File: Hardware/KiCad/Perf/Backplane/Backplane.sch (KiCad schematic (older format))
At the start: 10 parts, among them P1 CONN_02X20, P2 CONN_02X20, P3 CONN_02X16, P4 CONN_02X16, P5 CONN_02X16, P6 CONN_02X16, P7 CONN_02X16, P8 CONN_02X16, P9 CONN_02X16

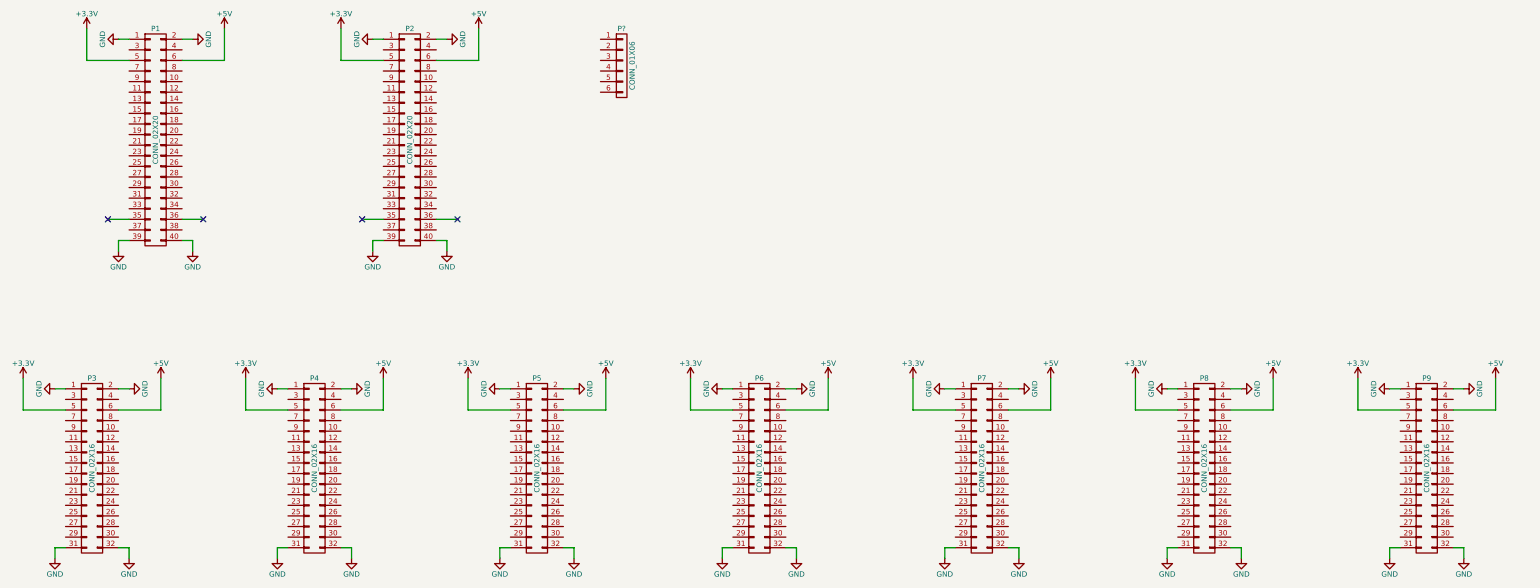
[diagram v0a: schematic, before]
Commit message: laying out motherboard and backplane
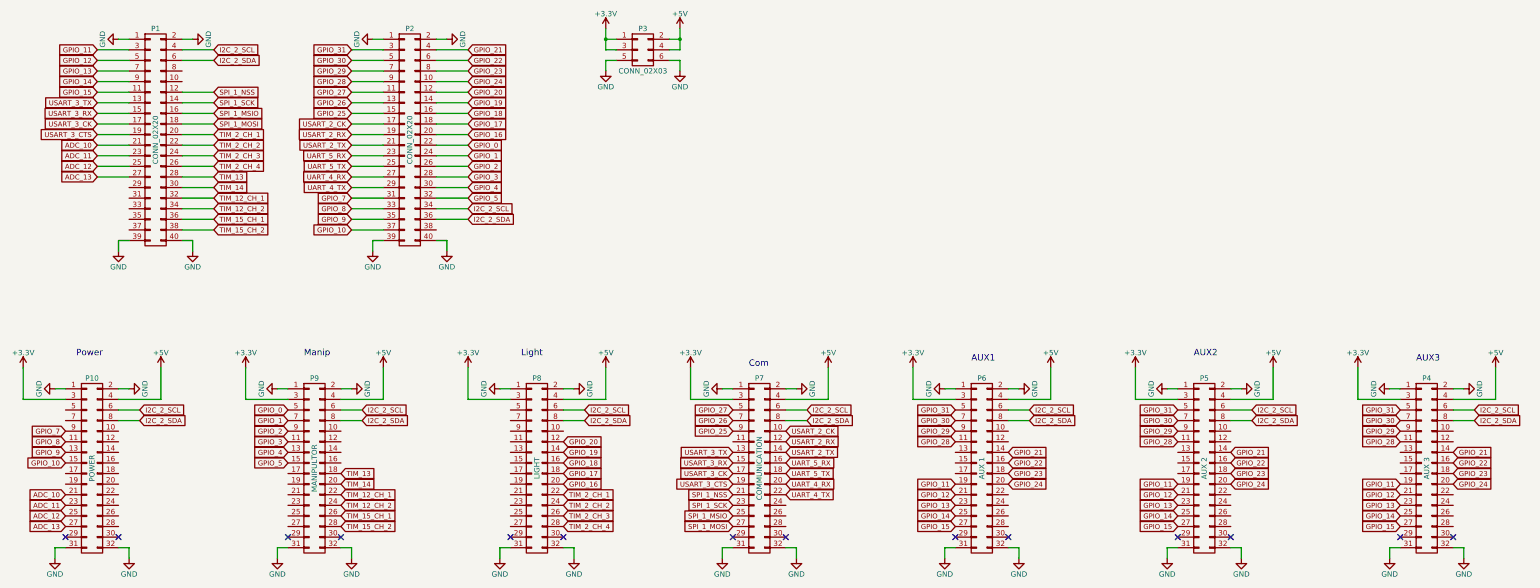
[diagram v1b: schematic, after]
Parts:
- removed P?: CONN_01X06, symbol CONN_01X06
- added P3: CONN_02X03, symbol CONN_02X03
- P10: renamed from P4; value CONN_02X16 -> POWER
- P4: renamed from P3; value CONN_02X16 -> AUX 3
- P5: renamed from P9; value CONN_02X16 -> AUX 2
- P6: renamed from P8; value CONN_02X16 -> AUX 1
- P7: value CONN_02X16 -> COMMUNICATION
- P8: renamed from P6; value CONN_02X16 -> LIGHT
- P9: renamed from P5; value CONN_02X16 -> MANIPULTOR
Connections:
- net +3V3: now also P10.3 (P3), P4.3 (P3), P5.3 (P3), P6.3 (P3), P7.3 (P3), P8.3 (P3), P9.3 (P3), P3.1 (P1), P3.3 (P3); no longer P1.5 (P5), P10.5 (P5), P2.5 (P5), P4.5 (P5), P5.5 (P5), P6.5 (P5), P7.5 (P5), P8.5 (P5), P9.5 (P5)
- net +5V: now also P10.4 (P4), P4.4 (P4), P5.4 (P4), P6.4 (P4), P7.4 (P4), P8.4 (P4), P9.4 (P4), P3.2 (P2), P3.4 (P4); no longer P1.6 (P6), P10.6 (P6), P2.6 (P6), P4.6 (P6), P5.6 (P6), P6.6 (P6), P7.6 (P6), P8.6 (P6), P9.6 (P6)
- net GND: now also P3.5 (P5), P3.6 (P6)
- net GPIO_28: now reaches P4.11 (P11)
- net GPIO_28: now also P2.9 (P9), P5.11 (P11), P6.11 (P11)
- net GPIO_21: now reaches P4.14 (P14)
- net GPIO_21: now also P2.4 (P4), P5.14 (P14), P6.14 (P14)
- net GPIO_22: now reaches P4.16 (P16)
- net GPIO_22: now also P2.6 (P6), P5.16 (P16), P6.16 (P16)
- net GPIO_23: now reaches P4.18 (P18)
- net GPIO_23: now also P2.8 (P8), P5.18 (P18), P6.18 (P18)
- net GPIO_11: now reaches P4.19 (P19)
- net GPIO_11: now also P1.3 (P3), P5.19 (P19), P6.19 (P19)
- net GPIO_24: now reaches P4.20 (P20)
- net GPIO_24: now also P2.10 (P10), P5.20 (P20), P6.20 (P20)
- net GPIO_12: now reaches P4.21 (P21)
- net GPIO_12: now also P1.5 (P5), P5.21 (P21), P6.21 (P21)
- net GPIO_13: now reaches P4.23 (P23)
- net GPIO_13: now also P1.7 (P7), P5.23 (P23), P6.23 (P23)
- net GPIO_14: now reaches P4.25 (P25)
- net GPIO_14: now also P1.9 (P9), P5.25 (P25), P6.25 (P25)
- net GPIO_15: now reaches P4.27 (P27)
- net GPIO_15: now also P1.11 (P11), P5.27 (P27), P6.27 (P27)
- net GPIO_30: now reaches P4.7 (P7)
- net GPIO_30: now also P2.5 (P5), P5.7 (P7), P6.7 (P7)
- net I2C_2_SDA: now reaches P4.8 (P8)
- net I2C_2_SDA: now also P1.6 (P6), P10.8 (P8), P2.36 (P36), P5.8 (P8), P6.8 (P8), P7.8 (P8), P8.8 (P8), P9.8 (P8)
- net GPIO_29: now reaches P4.9 (P9)
- net GPIO_29: now also P2.7 (P7), P5.9 (P9), P6.9 (P9)
- net GPIO_8: now reaches P10.11 (P11)
- net GPIO_8: now also P2.33 (P33)
- net GPIO_9: now reaches P10.13 (P13)
- net GPIO_9: now also P2.35 (P35)
- net GPIO_10: now reaches P10.15 (P15)
- net GPIO_10: now also P2.37 (P37)
- net ADC_10: now reaches P10.21 (P21)
- net ADC_10: now also P1.21 (P21)
- net ADC_11: now reaches P10.23 (P23)
- net ADC_11: now also P1.23 (P23)
- net ADC_12: now reaches P10.25 (P25)
- net ADC_12: now also P1.25 (P25)
- net ADC_13: now reaches P10.27 (P27)
- net ADC_13: now also P1.27 (P27)
- net GPIO_7: now reaches P10.9 (P9)
- net GPIO_7: now also P2.31 (P31)
- net GPIO_3: now reaches P9.11 (P11)
- net GPIO_3: now also P2.28 (P28)
- net GPIO_4: now reaches P9.13 (P13)
- net GPIO_4: now also P2.30 (P30)
- net GPIO_5: now reaches P9.15 (P15)
- net GPIO_5: now also P2.32 (P32)
- net TIM_13: now reaches P9.18 (P18)
- net TIM_13: now also P1.28 (P28)
- net TIM_14: now reaches P9.20 (P20)
- net TIM_14: now also P1.30 (P30)
- net TIM_12_CH_1: now reaches P9.22 (P22)
- net TIM_12_CH_1: now also P1.32 (P32)
- net TIM_12_CH_2: now reaches P9.24 (P24)
- net TIM_12_CH_2: now also P1.34 (P34)
- net TIM_15_CH_1: now reaches P9.26 (P26)
- net TIM_15_CH_1: now also P1.36 (P36)
- net TIM_15_CH_2: now reaches P9.28 (P28)
- net TIM_15_CH_2: now also P1.38 (P38)
- net GPIO_1: now reaches P9.7 (P7)
- net GPIO_1: now also P2.24 (P24)
- net GPIO_2: now reaches P9.9 (P9)
- net GPIO_2: now also P2.26 (P26)
- net GPIO_20: now reaches P8.12 (P12)
- net GPIO_20: now also P2.12 (P12)
- net GPIO_19: now reaches P8.14 (P14)
- net GPIO_19: now also P2.14 (P14)
- net GPIO_18: now reaches P8.16 (P16)
- net GPIO_18: now also P2.16 (P16)
- net GPIO_17: now reaches P8.18 (P18)
- net GPIO_17: now also P2.18 (P18)
- net GPIO_16: now reaches P8.20 (P20)
- net GPIO_16: now also P2.20 (P20)
- net TIM_2_CH_1: now reaches P8.22 (P22)
- net TIM_2_CH_1: now also P1.20 (P20)
- net TIM_2_CH_2: now reaches P8.24 (P24)
- net TIM_2_CH_2: now also P1.22 (P22)
- net TIM_2_CH_3: now reaches P8.26 (P26)
- net TIM_2_CH_3: now also P1.24 (P24)
- net TIM_2_CH_4: now reaches P8.28 (P28)
- net TIM_2_CH_4: now also P1.26 (P26)
- net USART_2_CK: now reaches P7.10 (P10)
- net USART_2_CK: now also P2.17 (P17)
- net USART_2_RX: now reaches P7.12 (P12)
- net USART_2_RX: now also P2.19 (P19)
- net USART_3_TX: now reaches P7.13 (P13)
- net USART_3_TX: now also P1.13 (P13)
- net USART_2_TX: now reaches P7.14 (P14)
- net USART_2_TX: now also P2.21 (P21)
- net USART_3_RX: now reaches P7.15 (P15)
- net USART_3_RX: now also P1.15 (P15)
- net UART_5_RX: now reaches P7.16 (P16)
- net UART_5_RX: now also P2.23 (P23)
- net USART_3_CK: now reaches P7.17 (P17)
- net USART_3_CK: now also P1.17 (P17)
- net UART_5_TX: now reaches P7.18 (P18)
- net UART_5_TX: now also P2.25 (P25)
- net USART_3_CTS: now reaches P7.19 (P19)
- net USART_3_CTS: now also P1.19 (P19)
- net UART_4_RX: now reaches P7.20 (P20)
- net UART_4_RX: now also P2.27 (P27)
- net SPI_1_NSS: now reaches P7.21 (P21)
- net SPI_1_NSS: now also P1.12 (P12)
- net UART_4_TX: now reaches P7.22 (P22)
- net UART_4_TX: now also P2.29 (P29)
- net SPI_1_SCK: now reaches P7.23 (P23)
- net SPI_1_SCK: now also P1.14 (P14)
- net SPI_1_MSIO: now reaches P7.25 (P25)
- net SPI_1_MSIO: now also P1.16 (P16)
- net SPI_1_MOSI: now reaches P7.27 (P27)
- net SPI_1_MOSI: now also P1.18 (P18)
- net GPIO_26: now reaches P7.7 (P7)
- net GPIO_26: now also P2.13 (P13)
- net GPIO_25: now reaches P7.9 (P9)
- net GPIO_25: now also P2.15 (P15)
- net I2C_2_SCL: now reaches P1.4 (P4)
- net I2C_2_SCL: now also P10.6 (P6), P2.34 (P34), P4.6 (P6), P5.6 (P6), P6.6 (P6), P7.6 (P6), P8.6 (P6), P9.6 (P6)
- net GPIO_27: now reaches P2.11 (P11)
- net GPIO_27: now also P7.5 (P5)
- net GPIO_0: now reaches P2.22 (P22)
- net GPIO_0: now also P9.5 (P5)
- net GPIO_31: now reaches P2.3 (P3)
- net GPIO_31: now also P4.5 (P5), P5.5 (P5), P6.5 (P5)
- no-connect marks 4 -> 14
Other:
- note added: "AUX1"
- note added: "AUX2"
- note added: "AUX3"
- note added: "Com"
- note added: "Light"
- note added: "Manip"
- note added: "Power"
- moved on the sheet: P10, P4, P5, P6, P7, P8, P9

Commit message: Small change to USART 2 pin layout from MB to Backplane
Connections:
- net GPIO_25: now also P2.11 (P11); no longer P2.15 (P15)
- net GPIO_26: now also P2.9 (P9); no longer P2.13 (P13)
- net GPIO_27: now also P2.7 (P7); no longer P2.11 (P11)
- net GPIO_28: now also P2.5 (P5); no longer P2.9 (P9)
- net GPIO_29: now also P2.3 (P3); no longer P2.7 (P7)
- net I2C_2_SCL: now also P1.8 (P8); no longer P1.4 (P4)
- net I2C_2_SDA: now also P1.10 (P10); no longer P1.6 (P6)
- net UART_4_RX: now also P7.24 (P24); no longer P7.20 (P20)
- net UART_4_TX: now also P7.26 (P26); no longer P7.22 (P22)
- net UART_5_RX: now also P7.20 (P20); no longer P7.16 (P16)
- net UART_5_TX: now also P7.22 (P22); no longer P7.18 (P18)
- net USART_2_CK: now also P2.13 (P13); no longer P2.17 (P17)
- net USART_2_RX: now also P2.15 (P15); no longer P2.19 (P19)
- net USART_2_TX: now also P2.17 (P17); no longer P2.21 (P21)
- removed net GPIO_30: P2.5 (P5), P4.7 (P7), P5.7 (P7), P6.7 (P7)
- removed net GPIO_31: P2.3 (P3), P4.5 (P5), P5.5 (P5), P6.5 (P5)
- new net USART_2_CTS: P2.21 (P21), P7.18 (P18)
- new net USART_2_RTS: P2.19 (P19), P7.16 (P16)
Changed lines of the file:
@@
 NoConn ~ 14500 6900
 NoConn ~ 15000 6900
-Text GLabel 3300 2300 2    47   Input ~ 0
-I2C_2_SCL
-Text GLabel 3300 2400 2    47   Input ~ 0
+Text GLabel 3300 2500 2    47   Input ~ 0
+I2C_2_SCL
+Text GLabel 3300 2600 2    47   Input ~ 0
 I2C_2_SDA
 Text GLabel 5700 3800 2    47   Input ~ 0
@@
 	15200 5800 15000 5800
 Wire Wire Line
-	3000 2300 3300 2300
-Wire Wire Line
-	3300 2400 3000 2400
+	3000 2500 3300 2500
+Wire Wire Line
+	3300 2600 3000 2600
 Wire Wire Line
 	5700 3800 5400 3800
@@
 Text GLabel 2200 3500 0    47   Input ~ 0
 ADC_13
+Text GLabel 4600 3200 0    47   Input ~ 0
+USART_2_CTS
+Text GLabel 4600 2900 0    47   Input ~ 0
+USART_2_RX
 Text GLabel 4600 3000 0    47   Input ~ 0
-USART_2_CK
-Text GLabel 4600 3100 0    47   Input ~ 0
-USART_2_RX
-Text GLabel 4600 3200 0    47   Input ~ 0
 USART_2_TX
 Text GLabel 4600 3300 0    47   Input ~ 0
@@
 GPIO_5
 Text GLabel 4600 2300 0    47   Input ~ 0
-GPIO_31
+GPIO_29
 Text GLabel 4600 2400 0    47   Input ~ 0
-GPIO_30
+GPIO_28
 Text GLabel 4600 2500 0    47   Input ~ 0
-GPIO_29
+GPIO_27
 Text GLabel 4600 2600 0    47   Input ~ 0
-GPIO_28
+GPIO_26
 Text GLabel 4600 2700 0    47   Input ~ 0
-GPIO_27
-Text GLabel 4600 2800 0    47   Input ~ 0
-GPIO_26
-Text GLabel 4600 2900 0    47   Input ~ 0
 GPIO_25
 Wire Wire Line
@@
 Text GLabel 12900 6400 2    47   Input ~ 0
 GPIO_24
-Text GLabel 12400 5700 0    47   Input ~ 0
-GPIO_31
-Text GLabel 12400 5800 0    47   Input ~ 0
-GPIO_30
 Text GLabel 12400 5900 0    47   Input ~ 0
 GPIO_29
@@
 Text GLabel 8700 6100 2    47   Input ~ 0
 USART_2_TX
-Text GLabel 8700 6200 2    47   Input ~ 0
+Text GLabel 8700 6400 2    47   Input ~ 0
 UART_5_RX
-Text GLabel 8700 6300 2    47   Input ~ 0
+Text GLabel 8700 6500 2    47   Input ~ 0
 UART_5_TX
-Text GLabel 8700 6400 2    47   Input ~ 0
+Text GLabel 8700 6600 2    47   Input ~ 0
 UART_4_RX
-Text GLabel 8700 6500 2    47   Input ~ 0
+Text GLabel 8700 6700 2    47   Input ~ 0
 UART_4_TX
 Text GLabel 10300 6400 0    47   Input ~ 0
@@
 Text GLabel 10300 6800 0    47   Input ~ 0
 GPIO_15
-Text GLabel 10300 5700 0    47   Input ~ 0
-GPIO_31
-Text GLabel 10300 5800 0    47   Input ~ 0
-GPIO_30
 Text GLabel 10300 5900 0    47   Input ~ 0
 GPIO_29
@@
 Text GLabel 14500 6800 0    47   Input ~ 0
 GPIO_15
-Text GLabel 14500 5700 0    47   Input ~ 0
-GPIO_31
-Text GLabel 14500 5800 0    47   Input ~ 0
-GPIO_30
 Text GLabel 14500 5900 0    47   Input ~ 0
 GPIO_29
@@
 Text GLabel 15000 6400 2    47   Input ~ 0
 GPIO_24
+Text GLabel 4600 3100 0    47   Input ~ 0
+USART_2_RTS
+Text GLabel 4600 2800 0    47   Input ~ 0
+USART_2_CK
+Text GLabel 8700 6300 2    47   Input ~ 0
+USART_2_CTS
+Text GLabel 8700 6200 2    47   Input ~ 0
+USART_2_RTS
 $EndSCHEMATC

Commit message: completed backplane pcb
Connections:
- net ADC_10: now also P10.11 (P11); no longer P10.21 (P21)
- net ADC_11: now also P10.9 (P9); no longer P10.23 (P23)
- net ADC_12: now also P10.7 (P7); no longer P10.25 (P25)
- net ADC_13: now also P10.5 (P5); no longer P10.27 (P27)
- net GPIO_0: now also P9.17 (P17); no longer P9.5 (P5)
- net GPIO_1: now also P9.19 (P19); no longer P9.7 (P7)
- net GPIO_10: now also P10.23 (P23); no longer P10.15 (P15)
- net GPIO_11: now also P4.13 (P13), P5.13 (P13), P6.13 (P13); no longer P4.19 (P19), P5.19 (P19), P6.19 (P19)
- net GPIO_12: now also P4.11 (P11), P5.11 (P11), P6.11 (P11); no longer P4.21 (P21), P5.21 (P21), P6.21 (P21)
- net GPIO_13: now also P4.9 (P9), P5.9 (P9), P6.9 (P9); no longer P4.23 (P23), P5.23 (P23), P6.23 (P23)
- net GPIO_14: now also P4.7 (P7), P5.7 (P7), P6.7 (P7); no longer P4.25 (P25), P5.25 (P25), P6.25 (P25)
- net GPIO_15: now also P4.5 (P5), P5.5 (P5), P6.5 (P5); no longer P4.27 (P27), P5.27 (P27), P6.27 (P27)
- net GPIO_16: now also P8.21 (P21); no longer P8.20 (P20)
- net GPIO_17: now also P8.19 (P19); no longer P8.18 (P18)
- net GPIO_18: now also P8.17 (P17); no longer P8.16 (P16)
- net GPIO_19: now also P8.15 (P15); no longer P8.14 (P14)
- net GPIO_2: now also P9.21 (P21); no longer P9.9 (P9)
- net GPIO_20: now also P8.13 (P13); no longer P8.12 (P12)
- net GPIO_21: now also P4.20 (P20), P5.20 (P20), P6.20 (P20); no longer P4.14 (P14), P5.14 (P14), P6.14 (P14)
- net GPIO_22: now also P4.18 (P18), P5.18 (P18), P6.18 (P18); no longer P4.16 (P16), P5.16 (P16), P6.16 (P16)
- net GPIO_23: now also P4.16 (P16), P5.16 (P16), P6.16 (P16); no longer P4.18 (P18), P5.18 (P18), P6.18 (P18)
- net GPIO_24: now also P4.14 (P14), P5.14 (P14), P6.14 (P14); no longer P4.20 (P20), P5.20 (P20), P6.20 (P20)
- net GPIO_25: now also P7.27 (P27); no longer P7.9 (P9)
- net GPIO_26: now also P7.25 (P25); no longer P7.7 (P7)
- net GPIO_27: now also P7.23 (P23); no longer P7.5 (P5)
- net GPIO_28: now also P4.21 (P21), P5.21 (P21), P6.21 (P21); no longer P4.11 (P11), P5.11 (P11), P6.11 (P11)
- net GPIO_29: now also P4.23 (P23), P5.23 (P23), P6.23 (P23); no longer P4.9 (P9), P5.9 (P9), P6.9 (P9)
- net GPIO_3: now also P9.23 (P23); no longer P9.11 (P11)
- net GPIO_4: now also P9.25 (P25); no longer P9.13 (P13)
- net GPIO_5: now also P9.27 (P27); no longer P9.15 (P15)
- net GPIO_7: now also P10.17 (P17); no longer P10.9 (P9)
- net GPIO_8: now also P10.19 (P19); no longer P10.11 (P11)
- net GPIO_9: now also P10.21 (P21); no longer P10.13 (P13)
- net I2C_2_SCL: now also P10.28 (P28), P4.28 (P28), P5.28 (P28), P6.28 (P28), P7.28 (P28), P8.28 (P28), P9.28 (P28); no longer P1.8 (P8), P10.6 (P6), P4.6 (P6), P5.6 (P6), P6.6 (P6), P7.6 (P6), P8.6 (P6), P9.6 (P6)
- net I2C_2_SDA: now also P10.26 (P26), P4.26 (P26), P5.26 (P26), P6.26 (P26), P7.26 (P26), P8.26 (P26), P9.26 (P26); no longer P1.10 (P10), P10.8 (P8), P4.8 (P8), P5.8 (P8), P6.8 (P8), P7.8 (P8), P8.8 (P8), P9.8 (P8)
- net SPI_1_MOSI: now also P7.5 (P5); no longer P7.27 (P27)
- net SPI_1_MSIO: now also P7.7 (P7); no longer P7.25 (P25)
- net SPI_1_NSS: now also P7.11 (P11); no longer P7.21 (P21)
- net SPI_1_SCK: now also P7.9 (P9); no longer P7.23 (P23)
- net TIM_12_CH_1: now also P9.12 (P12); no longer P9.22 (P22)
- net TIM_12_CH_2: now also P9.10 (P10); no longer P9.24 (P24)
- net TIM_13: now also P9.16 (P16); no longer P9.18 (P18)
- net TIM_14: now also P9.14 (P14); no longer P9.20 (P20)
- net TIM_15_CH_1: now also P9.8 (P8); no longer P9.26 (P26)
- net TIM_15_CH_2: now also P9.6 (P6); no longer P9.28 (P28)
- net TIM_2_CH_1: now also P8.12 (P12); no longer P8.22 (P22)
- net TIM_2_CH_2: now also P8.10 (P10); no longer P8.24 (P24)
- net TIM_2_CH_3: now also P8.8 (P8); no longer P8.26 (P26)
- net TIM_2_CH_4: now also P8.6 (P6); no longer P8.28 (P28)
- net UART_4_RX: now also P7.10 (P10); no longer P7.24 (P24)
- net UART_4_TX: now also P7.8 (P8); no longer P7.26 (P26)
- net UART_5_RX: now also P7.14 (P14); no longer P7.20 (P20)
- net UART_5_TX: now also P7.12 (P12); no longer P7.22 (P22)
- net USART_2_CK: now also P7.24 (P24); no longer P7.10 (P10)
- net USART_2_CTS: now also P7.16 (P16); no longer P7.18 (P18)
- net USART_2_RTS: now also P7.18 (P18); no longer P7.16 (P16)
- net USART_2_RX: now also P7.22 (P22); no longer P7.12 (P12)
- net USART_2_TX: now also P7.20 (P20); no longer P7.14 (P14)
- net USART_3_CK: now also P7.15 (P15); no longer P7.17 (P17)
- net USART_3_CTS: now also P7.13 (P13); no longer P7.19 (P19)
- net USART_3_RX: now also P7.17 (P17); no longer P7.15 (P15)
- net USART_3_TX: now also P7.19 (P19); no longer P7.13 (P13)
- no-connect marks 14 -> 18
